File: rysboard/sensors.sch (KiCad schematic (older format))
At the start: 9 parts, among them J10 ToF1, J11 ToF2, J12 ToF3, J13 ToF4, J14 SPI, J15 ToF5, J16 ToF6, J8 Temp, J9 IMU

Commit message: created eval board for STM , added mcu, created controll section for TOFS and FAN. Added programming pinout, Remooved legacy spi interface, Removed addidtional i2c socket
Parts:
- removed J14: SPI, Connector_Molex:Molex_PicoBlade_53047-0710_1x07_P1.25mm_Vertical, symbol Connector_Generic:Conn_01x07
- removed J8: Temp, Connector_Molex:Molex_PicoBlade_53047-0510_1x05_P1.25mm_Vertical, symbol Connector_Generic:Conn_01x05
- added Q?: DMP3036SSD-13, Package_SO:SO-8_5.3x6.2mm_P1.27mm, symbol rysboard:DMP3036SSD-13
- added Q?: NST847BDP6T5G, Package_TO_SOT_SMD:SOT-963, symbol rysboard:NST847BDP6T5G
- added R? (x2): R, symbol Device:R
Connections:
- net labels added: EN_TOFS
- net labels removed: SPI_CLK, SPI_CS, SPI_IRQ, SPI_MISO, SPI_MOSI
- wire segments 75 -> 64
- no-connect marks 2 -> 1
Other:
- note removed: "External SPI connector"
- note removed: "I2C temperature sensor connector"
- note removed: "Note: external sensor logic must be 3V3-level!"
- moved on the sheet: J9
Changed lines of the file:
@@
 $Descr A4 11693 8268
 encoding utf-8
-Sheet 4 6
+Sheet 5 7
 Title "rysboard"
 Date "2020-08-23"
@@
 Comment4 ""
 $EndDescr
-Text Notes 5000 2600 0    100  ~ 0
-External SPI connector
-Text Notes 4575 4700 0    100  ~ 0
-I2C temperature sensor connector
 Text Notes 1350 6250 0    100  ~ 0
 6x ToF I2C connector
@@
 Text HLabel 2350 2950 2    50   Input ~ 0
 TOF3_EN
-$Comp
-L Connector_Generic:Conn_01x07 J14
-U 1 1 5EE60C8D
-P 5550 1850
-F 0 "J14" H 5550 1450 50  0000 C CNN
-F 1 "SPI" H 5550 2250 50  0000 C CNN
-F 2 "Connector_Molex:Molex_PicoBlade_53047-0710_1x07_P1.25mm_Vertical" H 5550 1850 50  0001 C CNN
-F 3 "~" H 5550 1850 50  0001 C CNN
-	1    5550 1850
-	-1   0    0    1
-$EndComp
-$Comp
-L power:GND #PWR026
-U 1 1 5EE683DA
-P 5800 2200
-F 0 "#PWR026" H 5800 1950 50  0001 C CNN
-F 1 "GND" H 5805 2027 50  0000 C CNN
-F 2 "" H 5800 2200 50  0001 C CNN
-F 3 "" H 5800 2200 50  0001 C CNN
-	1    5800 2200
-	1    0    0    -1
-$EndComp
-Wire Wire Line
-	5800 2200 5800 2150
-Wire Wire Line
-	5800 2150 5750 2150
-Wire Wire Line
-	5750 1550 5800 1550
-Wire Wire Line
-	5800 1550 5800 1500
-Wire Wire Line
-	5750 2050 5850 2050
-Wire Wire Line
-	5750 1950 5850 1950
-Wire Wire Line
-	5750 1850 5850 1850
-Wire Wire Line
-	5750 1750 5850 1750
-Wire Wire Line
-	5750 1650 5850 1650
-Text HLabel 5850 1650 2    50   Input ~ 0
-SPI_MOSI
-Text HLabel 5850 1750 2    50   Output ~ 0
-SPI_MISO
-Text HLabel 5850 1850 2    50   Input ~ 0
-SPI_CLK
-Text HLabel 5850 1950 2    50   Input ~ 0
-SPI_CS
-Text HLabel 5850 2050 2    50   Output ~ 0
-SPI_IRQ
-$Comp
-L Connector_Generic:Conn_01x05 J8
-U 1 1 5EE7DCB5
-P 5550 4000
-F 0 "J8" H 5550 3700 50  0000 C CNN
-F 1 "Temp" H 5550 4300 50  0000 C CNN
-F 2 "Connector_Molex:Molex_PicoBlade_53047-0510_1x05_P1.25mm_Vertical" H 5550 4000 50  0001 C CNN
-F 3 "~" H 5550 4000 50  0001 C CNN
-	1    5550 4000
-	-1   0    0    1
-$EndComp
-Text HLabel 5850 4000 2    50   Input ~ 0
-I2C_SCL_TIMU
-Text HLabel 5850 3900 2    50   BiDi ~ 0
-I2C_SDA_TIMU
-Wire Wire Line
-	5750 3800 5800 3800
-Wire Wire Line
-	5800 3800 5800 3750
-$Comp
-L power:GND #PWR028
-U 1 1 5EE83D16
-P 5800 4250
-F 0 "#PWR028" H 5800 4000 50  0001 C CNN
-F 1 "GND" H 5805 4077 50  0000 C CNN
-F 2 "" H 5800 4250 50  0001 C CNN
-F 3 "" H 5800 4250 50  0001 C CNN
-	1    5800 4250
-	1    0    0    -1
-$EndComp
-Wire Wire Line
-	5800 4250 5800 4200
-Wire Wire Line
-	5800 4200 5750 4200
-Wire Wire Line
-	5750 4000 5850 4000
-Wire Wire Line
-	5750 3900 5850 3900
-NoConn ~ 5750 4100
-Text Notes 5075 6675 0    100  ~ 0
+Text Notes 3325 6275 0    100  ~ 0
 I2C IMU connector
 $Comp
 L Connector_Generic:Conn_01x05 J9
 U 1 1 5EE95D68
-P 5550 6000
-F 0 "J9" H 5550 5700 50  0000 C CNN
-F 1 "IMU" H 5550 6300 50  0000 C CNN
-F 2 "Connector_Molex:Molex_PicoBlade_53047-0510_1x05_P1.25mm_Vertical" H 5550 6000 50  0001 C CNN
-F 3 "~" H 5550 6000 50  0001 C CNN
-	1    5550 6000
-	-1   0    0    1
-$EndComp
-Text HLabel 5850 6000 2    50   Input ~ 0
+P 3800 5600
+F 0 "J9" H 3800 5300 50  0000 C CNN
+F 1 "IMU" H 3800 5900 50  0000 C CNN
+F 2 "Connector_Molex:Molex_PicoBlade_53047-0510_1x05_P1.25mm_Vertical" H 3800 5600 50  0001 C CNN
+F 3 "~" H 3800 5600 50  0001 C CNN
+	1    3800 5600
+	-1   0    0    1
+$EndComp
+Text HLabel 4100 5600 2    50   Input ~ 0
 I2C_SCL_TIMU
-Text HLabel 5850 5900 2    50   BiDi ~ 0
+Text HLabel 4100 5500 2    50   BiDi ~ 0
 I2C_SDA_TIMU
 Wire Wire Line
-	5750 5800 5800 5800
-Wire Wire Line
-	5800 5800 5800 5750
+	4000 5400 4050 5400
+Wire Wire Line
+	4050 5400 4050 5350
 $Comp
 L power:GND #PWR030
 U 1 1 5EE95D78
-P 5800 6250
-F 0 "#PWR030" H 5800 6000 50  0001 C CNN
-F 1 "GND" H 5805 6077 50  0000 C CNN
-F 2 "" H 5800 6250 50  0001 C CNN
-F 3 "" H 5800 6250 50  0001 C CNN
-	1    5800 6250
-	1    0    0    -1
-$EndComp
-Wire Wire Line
-	5800 6250 5800 6200
-Wire Wire Line
-	5800 6200 5750 6200
-Wire Wire Line
-	5750 6000 5850 6000
-Wire Wire Line
-	5750 5900 5850 5900
+P 4050 5850
+F 0 "#PWR030" H 4050 5600 50  0001 C CNN
+F 1 "GND" H 4055 5677 50  0000 C CNN
+F 2 "" H 4050 5850 50  0001 C CNN
+F 3 "" H 4050 5850 50  0001 C CNN
+	1    4050 5850
+	1    0    0    -1
+$EndComp
+Wire Wire Line
+	4050 5850 4050 5800
+Wire Wire Line
+	4050 5800 4000 5800
+Wire Wire Line
+	4000 5600 4100 5600
+Wire Wire Line
+	4000 5500 4100 5500
 Text HLabel 2300 3900 2    50   Input ~ 0
 I2C_SCL_TOF1
 Text HLabel 2300 3800 2    50   BiDi ~ 0
 I2C_SDA_TOF1
-NoConn ~ 5750 6100
+NoConn ~ 4000 5700
 $Comp
 L power:GND #PWR0110
@@
 $EndComp
 $Comp
-L power:+5V #PWR0109
-U 1 1 5ECB9E16
-P 5800 3750
-F 0 "#PWR0109" H 5800 3600 50  0001 C CNN
-F 1 "+5V" H 5815 3923 50  0000 C CNN
-F 2 "" H 5800 3750 50  0001 C CNN
-F 3 "" H 5800 3750 50  0001 C CNN
-	1    5800 3750
-	1    0    0    -1
-$EndComp
-$Comp
-L power:+5V #PWR0111
-U 1 1 5ECBB5E8
-P 5800 1500
-F 0 "#PWR0111" H 5800 1350 50  0001 C CNN
-F 1 "+5V" H 5815 1673 50  0000 C CNN
-F 2 "" H 5800 1500 50  0001 C CNN
-F 3 "" H 5800 1500 50  0001 C CNN
-	1    5800 1500
-	1    0    0    -1
-$EndComp
-$Comp
 L power:+5V #PWR0112
 U 1 1 5ECBCED2
-P 5800 5750
-F 0 "#PWR0112" H 5800 5600 50  0001 C CNN
-F 1 "+5V" H 5815 5923 50  0000 C CNN
-F 2 "" H 5800 5750 50  0001 C CNN
-F 3 "" H 5800 5750 50  0001 C CNN
-	1    5800 5750
-	1    0    0    -1
-$EndComp
-Text Notes 6350 1300 0    50   ~ 0
-Note: external sensor logic must be 3V3-level!
-Text GLabel 2200 3700 2    50   Input ~ 0
-TOF_5V
+P 4050 5350
+F 0 "#PWR0112" H 4050 5200 50  0001 C CNN
+F 1 "+5V" H 4065 5523 50  0000 C CNN
+F 2 "" H 4050 5350 50  0001 C CNN
+F 3 "" H 4050 5350 50  0001 C CNN
+	1    4050 5350
+	1    0    0    -1
+$EndComp
 Wire Wire Line
 	2300 3800 2100 3800
@@
 Wire Wire Line
 	2050 4400 2050 3700
-Wire Wire Line
-	2200 3700 2050 3700
 Connection ~ 2050 3700
 Wire Wire Line
@@
 Wire Wire Line
 	2150 1350 1650 1350
-Text GLabel 2350 1250 2    50   Input ~ 0
-TOF_5V
 Wire Wire Line
 	1650 1250 2100 1250
@@
 Connection ~ 2100 1250
 Wire Wire Line
-	2100 1250 2350 1250
-Wire Wire Line
 	2100 1950 2100 2650
 Wire Wire Line
@@
 Wire Wire Line
 	2200 2150 2200 2850
+Text Label 2650 1250 2    50   ~ 0
+TOF_5V
+Wire Wire Line
+	2100 1250 2650 1250
+Text Label 2600 3700 2    50   ~ 0
+TOF_5V
+Wire Wire Line
+	2050 3700 2600 3700
+$Comp
+L rysboard:DMP3036SSD-13 Q?
+U 1 1 6035FE64
+P 5250 1350
+F 0 "Q?" V 5592 1350 50  0000 C CNN
+F 1 "DMP3036SSD-13" V 5501 1350 50  0000 C CNN
+F 2 "Package_SO:SO-8_5.3x6.2mm_P1.27mm" H 5450 1275 50  0001 L CIN
+F 3 "http://www.vishay.com/docs/70209/70209.pdf" H 5250 1350 50  0001 L CNN
+	1    5250 1350
+	0    1    -1   0
+$EndComp
+$Comp
+L power:+5V #PWR?
+U 1 1 6036243F
+P 4700 1250
+F 0 "#PWR?" H 4700 1100 50  0001 C CNN
+F 1 "+5V" H 4715 1423 50  0000 C CNN
+F 2 "" H 4700 1250 50  0001 C CNN
+F 3 "" H 4700 1250 50  0001 C CNN
+	1    4700 1250
+	1    0    0    -1
+$EndComp
+$Comp
+L power:GND #PWR?
+U 1 1 60362AB5
+P 4900 1950
+F 0 "#PWR?" H 4900 1700 50  0001 C CNN
+F 1 "GND" H 4905 1777 50  0000 C CNN
+F 2 "" H 4900 1950 50  0001 C CNN
+F 3 "" H 4900 1950 50  0001 C CNN
+	1    4900 1950
+	1    0    0    -1
+$EndComp
+$Comp
+L Device:R R?
+U 1 1 6036320A
+P 4900 1400
+F 0 "R?" H 4970 1446 50  0000 L CNN
+F 1 "R" H 4970 1355 50  0000 L CNN
+F 2 "" V 4830 1400 50  0001 C CNN
+F 3 "~" H 4900 1400 50  0001 C CNN
+	1    4900 1400
+	1    0    0    -1
+$EndComp
+Wire Wire Line
+	4900 1250 5050 1250
+Connection ~ 4900 1250
+Wire Wire Line
+	4900 1250 4700 1250
+$Comp
+L Device:R R?
+U 1 1 60366827
+P 4450 1750
+F 0 "R?" V 4243 1750 50  0000 C CNN
+F 1 "R" V 4334 1750 50  0000 C CNN
+F 2 "" V 4380 1750 50  0001 C CNN
+F 3 "~" H 4450 1750 50  0001 C CNN
+	1    4450 1750
+	0    1    1    0
+$EndComp
+Wire Wire Line
+	5250 1550 4900 1550
+$Comp
+L rysboard:NST847BDP6T5G Q?
+U 2 1 60369052
+P 4800 1750
+F 0 "Q?" H 4990 1796 50  0000 L CNN
+F 1 "NST847BDP6T5G" H 4990 1705 50  0000 L CNN
+F 2 "Package_TO_SOT_SMD:SOT-963" H 5000 1850 50  0001 C CNN
+F 3 "~" H 4800 1750 50  0001 C CNN
+	2    4800 1750
+	1    0    0    -1
+$EndComp
+Connection ~ 4900 1550
+Text HLabel 4300 1750 0    50   Output ~ 0
+EN_TOFS
+Text Label 5700 1250 0    50   ~ 0
+TOF_5V
+Wire Wire Line
+	5700 1250 5450 1250
 $EndSCHEMATC

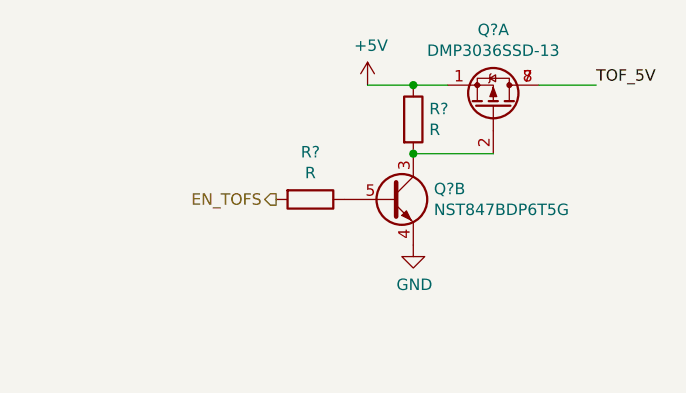
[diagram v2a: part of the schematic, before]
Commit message: added some of the analog sensors
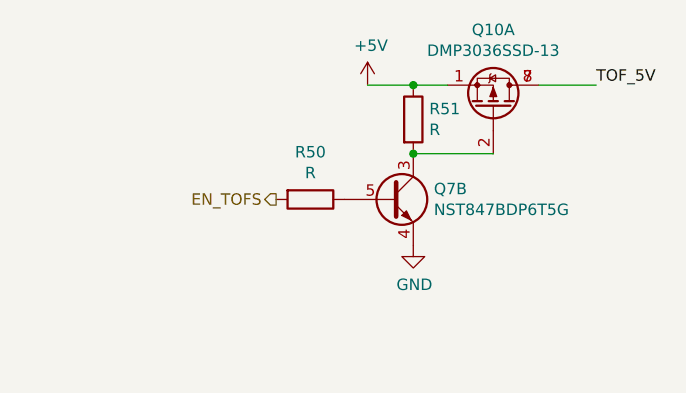
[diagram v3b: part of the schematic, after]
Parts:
- gave numbers to parts that had none: 4
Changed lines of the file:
@@
 	2050 3700 2600 3700
 $Comp
-L rysboard:DMP3036SSD-13 Q?
+L rysboard:DMP3036SSD-13 Q10
 U 1 1 6035FE64
 P 5250 1350
-F 0 "Q?" V 5592 1350 50  0000 C CNN
+F 0 "Q10" V 5592 1350 50  0000 C CNN
 F 1 "DMP3036SSD-13" V 5501 1350 50  0000 C CNN
 F 2 "Package_SO:SO-8_5.3x6.2mm_P1.27mm" H 5450 1275 50  0001 L CIN
@@
 $EndComp
 $Comp
-L power:+5V #PWR?
+L power:+5V #PWR0102
 U 1 1 6036243F
 P 4700 1250
-F 0 "#PWR?" H 4700 1100 50  0001 C CNN
+F 0 "#PWR0102" H 4700 1100 50  0001 C CNN
 F 1 "+5V" H 4715 1423 50  0000 C CNN
 F 2 "" H 4700 1250 50  0001 C CNN
@@
 $EndComp
 $Comp
-L power:GND #PWR?
+L power:GND #PWR0103
 U 1 1 60362AB5
 P 4900 1950
-F 0 "#PWR?" H 4900 1700 50  0001 C CNN
+F 0 "#PWR0103" H 4900 1700 50  0001 C CNN
 F 1 "GND" H 4905 1777 50  0000 C CNN
 F 2 "" H 4900 1950 50  0001 C CNN
@@
 $EndComp
 $Comp
-L Device:R R?
+L Device:R R51
 U 1 1 6036320A
 P 4900 1400
-F 0 "R?" H 4970 1446 50  0000 L CNN
+F 0 "R51" H 4970 1446 50  0000 L CNN
 F 1 "R" H 4970 1355 50  0000 L CNN
 F 2 "" V 4830 1400 50  0001 C CNN
@@
 	4900 1250 4700 1250
 $Comp
-L Device:R R?
+L Device:R R50
 U 1 1 60366827
 P 4450 1750
-F 0 "R?" V 4243 1750 50  0000 C CNN
+F 0 "R50" V 4243 1750 50  0000 C CNN
 F 1 "R" V 4334 1750 50  0000 C CNN
 F 2 "" V 4380 1750 50  0001 C CNN
@@
 	5250 1550 4900 1550
 $Comp
-L rysboard:NST847BDP6T5G Q?
+L rysboard:NST847BDP6T5G Q7
 U 2 1 60369052
 P 4800 1750
-F 0 "Q?" H 4990 1796 50  0000 L CNN
+F 0 "Q7" H 4990 1796 50  0000 L CNN
 F 1 "NST847BDP6T5G" H 4990 1705 50  0000 L CNN
 F 2 "Package_TO_SOT_SMD:SOT-963" H 5000 1850 50  0001 C CNN

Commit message: Fixed library, added a few MOSFET layouts
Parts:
- removed Q10: DMP3036SSD-13, Package_SO:SO-8_5.3x6.2mm_P1.27mm, symbol rysboard:DMP3036SSD-13
- added Q?: DMP2075UFDB, SamacSys_Parts:DMP2075UFDB7, symbol rysboard:DMP2075UFDB
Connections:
- net +5V: now also Q?.3 (S2)
- net TOF_5V: now also Q?.3 (S2), Q?.8 (D2_2)
- net at Q7.3 (C2), R51.2: now also Q?.4 (G2)
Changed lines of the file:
@@
 	2050 3700 2600 3700
-$Comp
-L rysboard:DMP3036SSD-13 Q10
-U 1 1 6035FE64
-P 5250 1350
-F 0 "Q10" V 5592 1350 50  0000 C CNN
-F 1 "DMP3036SSD-13" V 5501 1350 50  0000 C CNN
-F 2 "Package_SO:SO-8_5.3x6.2mm_P1.27mm" H 5450 1275 50  0001 L CIN
-F 3 "http://www.vishay.com/docs/70209/70209.pdf" H 5250 1350 50  0001 L CNN
-	1    5250 1350
-	0    1    -1   0
-$EndComp
 $Comp
 L power:+5V #PWR0102
@@
 Wire Wire Line
 	5700 1250 5450 1250
+$Comp
+L rysboard:DMP2075UFDB Q?
+U 2 1 605EBA08
+P 5250 1350
+F 0 "Q?" V 5592 1350 50  0000 C CNN
+F 1 "DMP2075UFDB" V 5501 1350 50  0000 C CNN
+F 2 "SamacSys_Parts:DMP2075UFDB7" H 5450 1275 50  0001 L CIN
+F 3 "" H 5250 1350 50  0001 L CNN
+	2    5250 1350
+	0    1    -1   0
+$EndComp
 $EndSCHEMATC

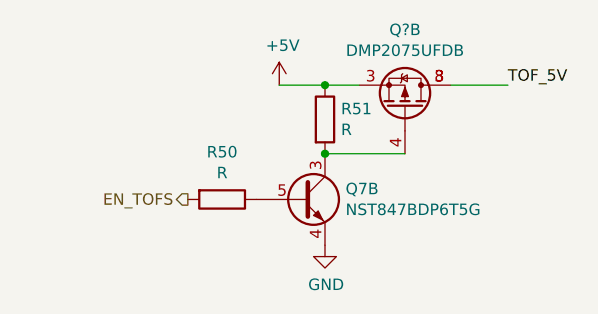
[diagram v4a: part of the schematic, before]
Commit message: battery Balancing specified
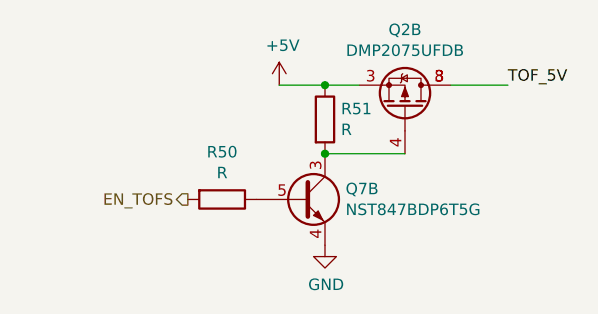
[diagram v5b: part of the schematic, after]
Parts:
- gave numbers to parts that had none: 1
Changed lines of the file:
@@
 	5700 1250 5450 1250
 $Comp
-L rysboard:DMP2075UFDB Q?
+L rysboard:DMP2075UFDB Q2
 U 2 1 605EBA08
 P 5250 1350
-F 0 "Q?" V 5592 1350 50  0000 C CNN
+F 0 "Q2" V 5592 1350 50  0000 C CNN
 F 1 "DMP2075UFDB" V 5501 1350 50  0000 C CNN
 F 2 "SamacSys_Parts:DMP2075UFDB7" H 5450 1275 50  0001 L CIN

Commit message: more footprints
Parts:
- R50: value R -> 1KR; footprint (none) -> Resistor_SMD:R_0603_1608Metric
- R51: value R -> 10KR; footprint (none) -> Resistor_SMD:R_0603_1608Metric
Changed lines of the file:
@@
 P 4900 1400
 F 0 "R51" H 4970 1446 50  0000 L CNN
-F 1 "R" H 4970 1355 50  0000 L CNN
-F 2 "" V 4830 1400 50  0001 C CNN
+F 1 "10KR" H 4970 1355 50  0000 L CNN
+F 2 "Resistor_SMD:R_0603_1608Metric" V 4830 1400 50  0001 C CNN
 F 3 "~" H 4900 1400 50  0001 C CNN
 	1    4900 1400
@@
 Wire Wire Line
 	4900 1250 4700 1250
-$Comp
-L Device:R R50
-U 1 1 60366827
-P 4450 1750
-F 0 "R50" V 4243 1750 50  0000 C CNN
-F 1 "R" V 4334 1750 50  0000 C CNN
-F 2 "" V 4380 1750 50  0001 C CNN
-F 3 "~" H 4450 1750 50  0001 C CNN
-	1    4450 1750
-	0    1    1    0
-$EndComp
 Wire Wire Line
 	5250 1550 4900 1550
@@
 	0    1    -1   0
 $EndComp
+$Comp
+L Device:R R50
+U 1 1 60445DB9
+P 4450 1750
+F 0 "R50" H 4520 1796 50  0000 L CNN
+F 1 "1KR" H 4520 1705 50  0000 L CNN
+F 2 "Resistor_SMD:R_0603_1608Metric" V 4380 1750 50  0001 C CNN
+F 3 "~" H 4450 1750 50  0001 C CNN
+	1    4450 1750
+	0    1    1    0
+$EndComp
 $EndSCHEMATC

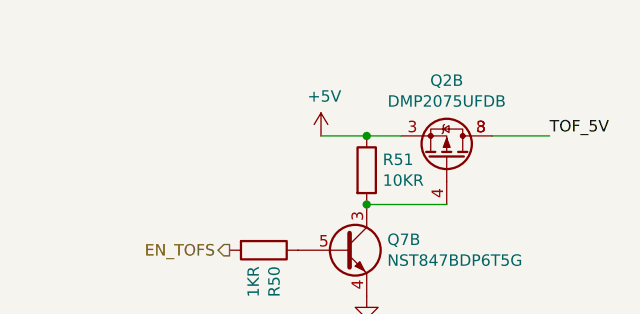
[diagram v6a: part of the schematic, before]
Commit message: More Work. RPI can now programm STM32 via GPIO
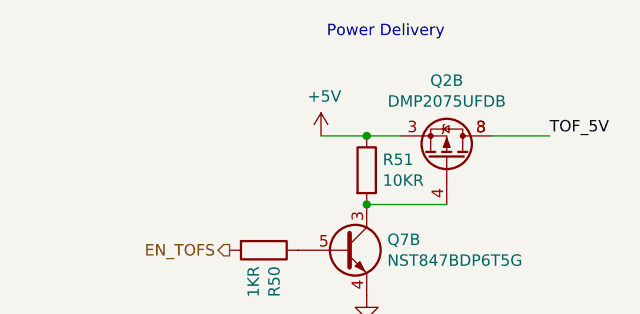
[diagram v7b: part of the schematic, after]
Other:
- note added: "Power Delivery\n"
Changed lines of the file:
@@
 $Descr A4 11693 8268
 encoding utf-8
-Sheet 5 7
+Sheet 7 7
 Title "rysboard"
 Date "2020-08-23"
@@
 	0    1    1    0
 $EndComp
+Text Notes 4725 825  0    50   ~ 0
+Power Delivery\n
 $EndSCHEMATC

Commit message: Bom finished pcb cleanup started
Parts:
- removed Q2: DMP2075UFDB, SamacSys_Parts:DMP2075UFDB7, symbol rysboard:DMP2075UFDB
- added Q11: AO3401A, Package_TO_SOT_SMD:SOT-23, symbol Transistor_FET:AO3401A
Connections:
- net +5V: now also Q11.2 (S)
- net TOF_5V: now also Q11.3 (D)
- net at Q7.3 (C2), R51.2: now also Q11.1 (G)
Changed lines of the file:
@@
 	5700 1250 5450 1250
-$Comp
-L rysboard:DMP2075UFDB Q2
-U 2 1 605EBA08
-P 5250 1350
-F 0 "Q2" V 5592 1350 50  0000 C CNN
-F 1 "DMP2075UFDB" V 5501 1350 50  0000 C CNN
-F 2 "SamacSys_Parts:DMP2075UFDB7" H 5450 1275 50  0001 L CIN
-F 3 "" H 5250 1350 50  0001 L CNN
-	2    5250 1350
-	0    1    -1   0
-$EndComp
 $Comp
 L Device:R R50
@@
 Text Notes 4725 825  0    50   ~ 0
 Power Delivery\n
+$Comp
+L Transistor_FET:AO3401A Q11
+U 1 1 608DDCED
+P 5250 1350
+F 0 "Q11" V 5592 1350 50  0000 C CNN
+F 1 "AO3401A" V 5501 1350 50  0000 C CNN
+F 2 "Package_TO_SOT_SMD:SOT-23" H 5450 1275 50  0001 L CIN
+F 3 "http://www.aosmd.com/pdfs/datasheet/AO3401A.pdf" H 5250 1350 50  0001 L CNN
+	1    5250 1350
+	0    1    -1   0
+$EndComp
 $EndSCHEMATC
